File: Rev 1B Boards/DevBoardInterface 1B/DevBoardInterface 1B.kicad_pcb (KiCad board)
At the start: 4 copper layers, 45.6 x 65 mm, 27 parts, among them J11 Banana 2P, J12 Banana 2P, J13 Banana 2P, J3 Conn_01x01_Pin, J6 JST4_F, J9 Conn_01x01_Pin, U10 ADS1014IDGS, U6 ISO164xB, U7 ADS1014IDGS, U8 TLV9301xDBV, U9 DAC53401

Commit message: More layout
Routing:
- net /Dev Board Interface/SCL_{INT}: track 0.00 -> 38.5 mm
- net /+3V3_{DEV}: track 0.00 -> 10.7 mm
- net /Dev Board Interface/SDA_{INT}: track 0.00 -> 10.7 mm
- net /SDA_{IN}: track 0.00 -> 10.4 mm
- net /SCL_{IN}: track 0.00 -> 10.4 mm
- net /+6V_{SCAP}_ADC: track 0.00 -> 9.09 mm
- net GNDPWR: track 0.00 -> 9.06 mm
- net /Dev Board Interface/V_{SC}_scaled: track 0.00 -> 8.17 mm
- net +3V3: track 0.00 -> 4.40 mm
- added copper zone on In2.Cu, net +24V
- added copper zone on F.Cu, net +3V3
- added copper zone on B.Cu, net GND
- added copper zone on In1.Cu, net GND
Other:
- board text added: "+ 24V -"
- board text added: "+ 3V3 -"
- board text added: "+ SCAP -"

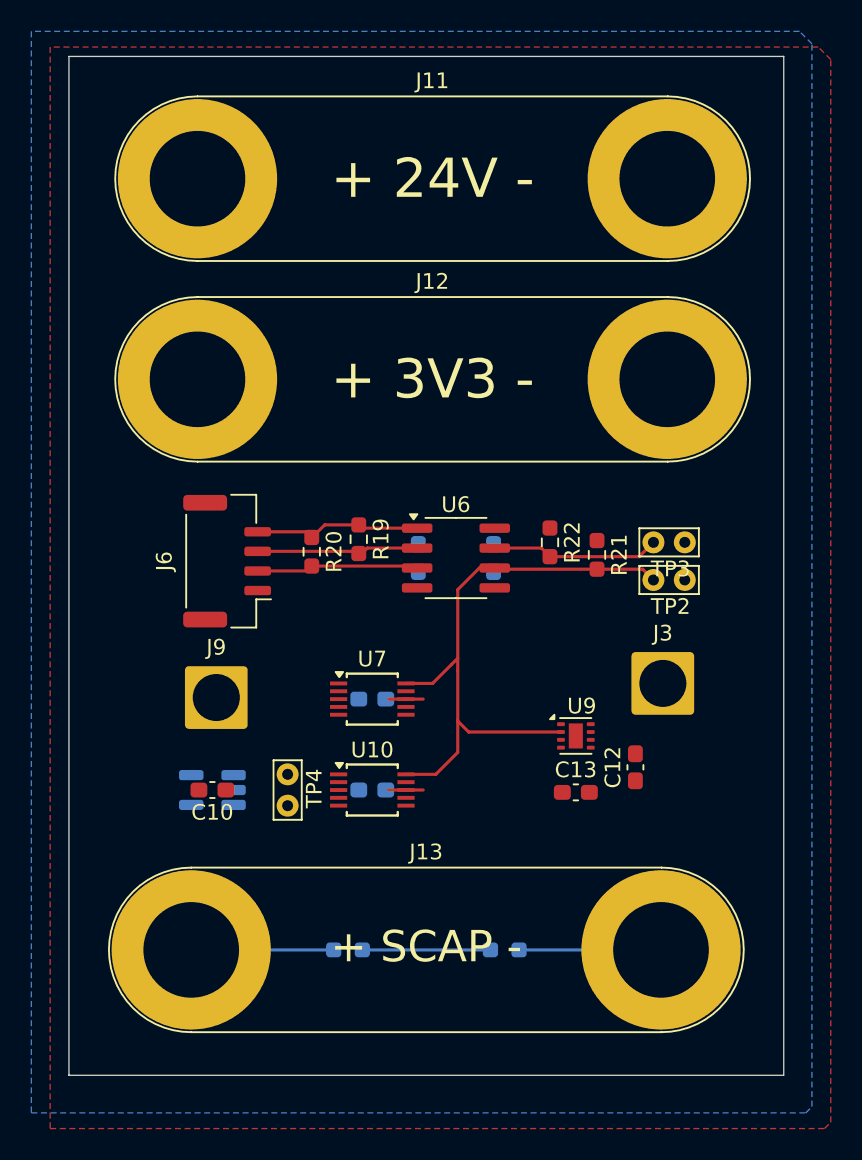
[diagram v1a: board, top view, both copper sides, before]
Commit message: Complete dev board interface layout
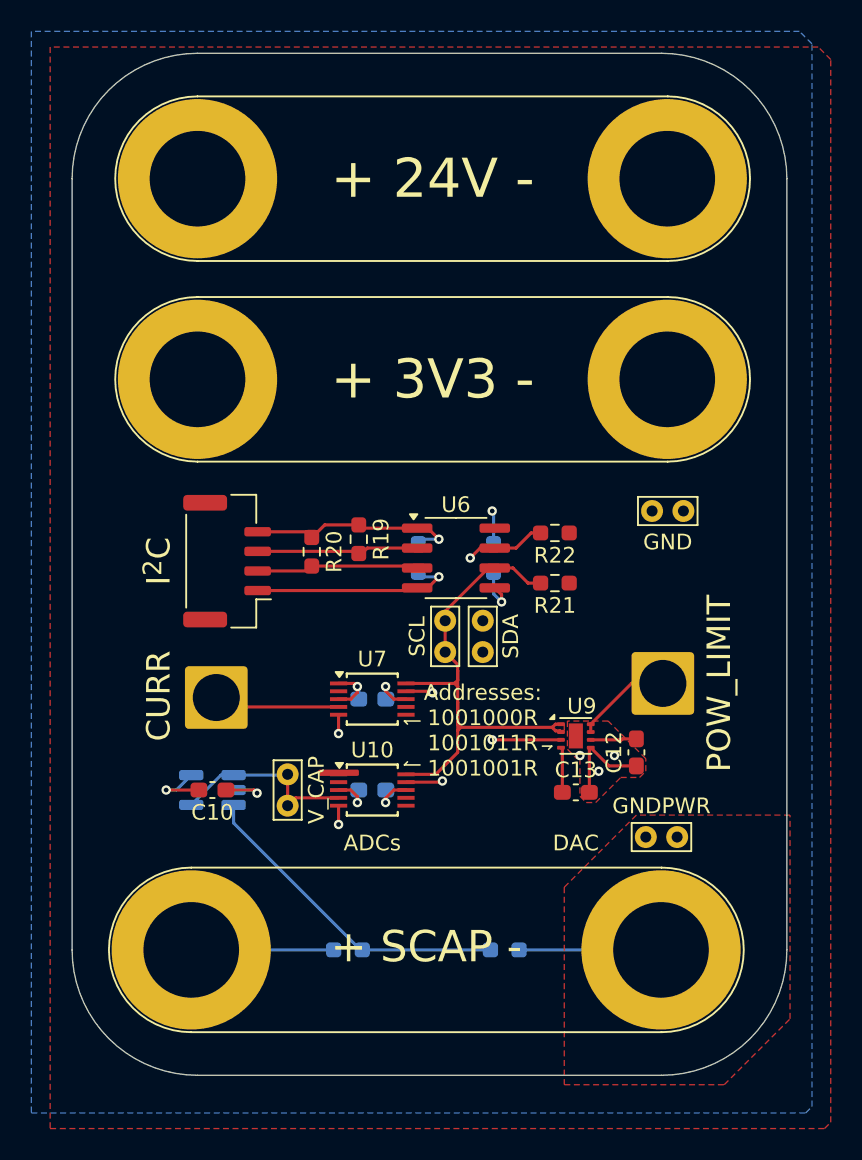
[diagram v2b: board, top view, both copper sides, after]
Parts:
- added G***: LOGO, ! Robomaster Special:StampedeLogo, B.Cu at (178.0, 59.6)
- added TP5: Loop TP, TestPoint:TestPoint_Bridge_Pitch2.0mm_Drill0.7mm, F.Cu at (192.2, 80.2)
- added TP6: Loop TP, TestPoint:TestPoint_Bridge_Pitch2.0mm_Drill0.7mm, F.Cu at (191.8, 101.0)
- moved TP2 14.1 mm to (179.0, 89.2), turned to 90 degrees
- moved TP3 12.9 mm to (181.4, 89.2), turned to 90 degrees
- moved R21 3.23 mm to (186.0, 84.8), turned to 180 degrees
- moved C12 0.95 mm to (191.2, 95.6)
- moved R22 0.68 mm to (186.0, 81.6), turned to 180 degrees
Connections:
- U9 pad 1: +3V3 -> /Dev Board Interface/SCL_{INT}
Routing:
- net GNDPWR: track 9.06 -> 51.5 mm, vias 0 -> 3
- net /Dev Board Interface/SDA_{INT}: track 10.7 -> 35.3 mm, vias 0 -> 4
- net GND: track 0.00 -> 16.0 mm, vias 0 -> 6
- net GNDD: track 0.00 -> 13.4 mm, vias 0 -> 1
- net /Dev Board Interface/V_{SC}_scaled: track 8.17 -> 20.9 mm
- net /Dev Board Interface/V_{SC}_BUF: track 0.00 -> 12.4 mm
- net /CURR_IN: track 0.00 -> 8.05 mm
- net /POW_LIMIT_OUT: track 0.00 -> 6.18 mm
- net +3V3: track 4.40 -> 10.3 mm, vias 0 -> 3
- net /Dev Board Interface/SCL_{INT}: track 38.5 -> 34.3 mm
- net +24V: track 0.00 -> 4.08 mm, vias 0 -> 1
- net /+3V3_{DEV}: track 10.7 -> 13.9 mm, vias 0 -> 1
- net /Dev Board Interface/CAP_{1}: track 0.00 -> 2.89 mm
- added copper zone on F.Cu, net /Dev Board Interface/SCL_{INT}
- added copper zone on F.Cu, net GND
- added copper zone on F.Cu, net GNDPWR
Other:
- board size 45.6 x 65 mm -> 45.6 x 65.2 mm
- board text added: "+3V3 SDA SCL GND"
- board text added: "ADCs"
- board text added: "Addresses: 1001000R 1001011R 1001001R"
- board text added: "CURR"
- board text added: "DAC"
- board text added: "GND"
- board text added: "GNDPWR"
- board text added: "I^{2}C"
- board text added: "POW_LIMIT"
- board text added: "SCL"
- board text added: "SDA"
- board text added: "UT Stampede Supercap Dev Board Interface _{Egan Wang, Jed Wang}"
- board text added: "V_CAP"

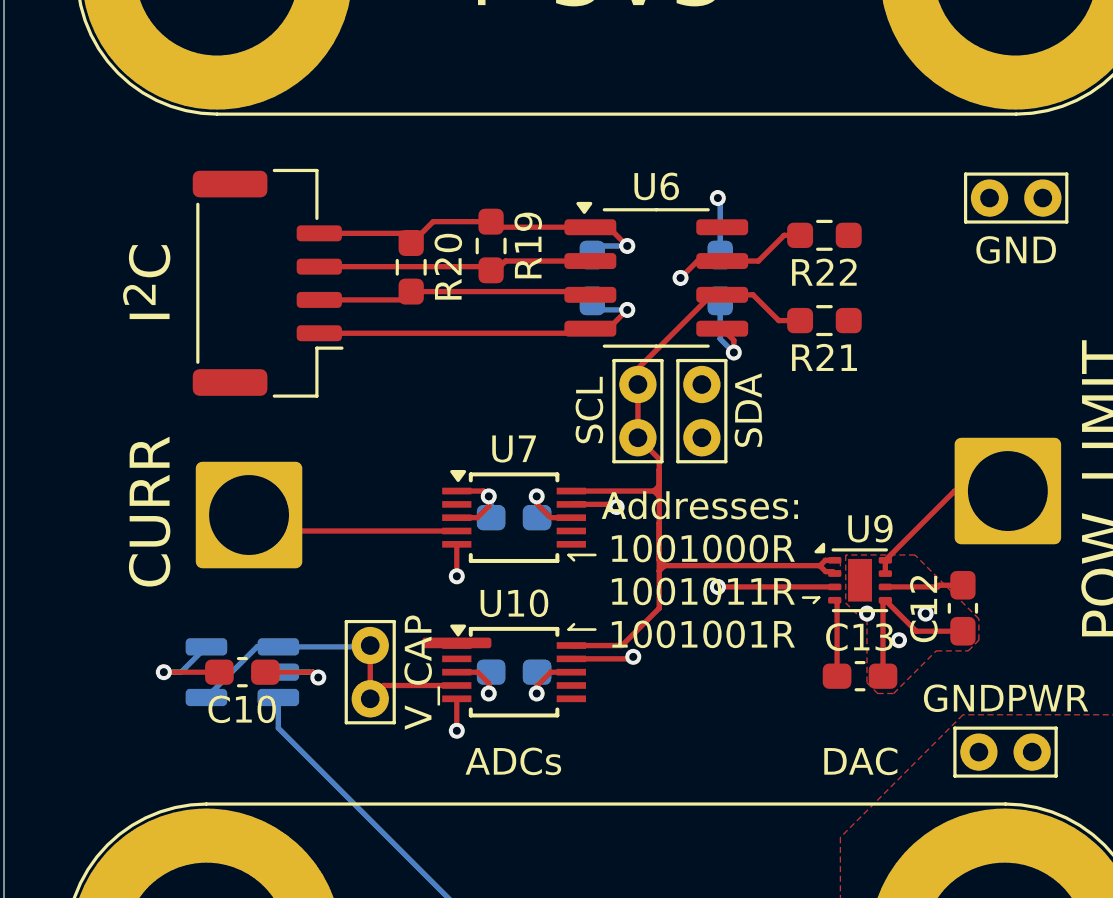
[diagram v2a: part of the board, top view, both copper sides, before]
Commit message: Update PCB to fix ERC breaks
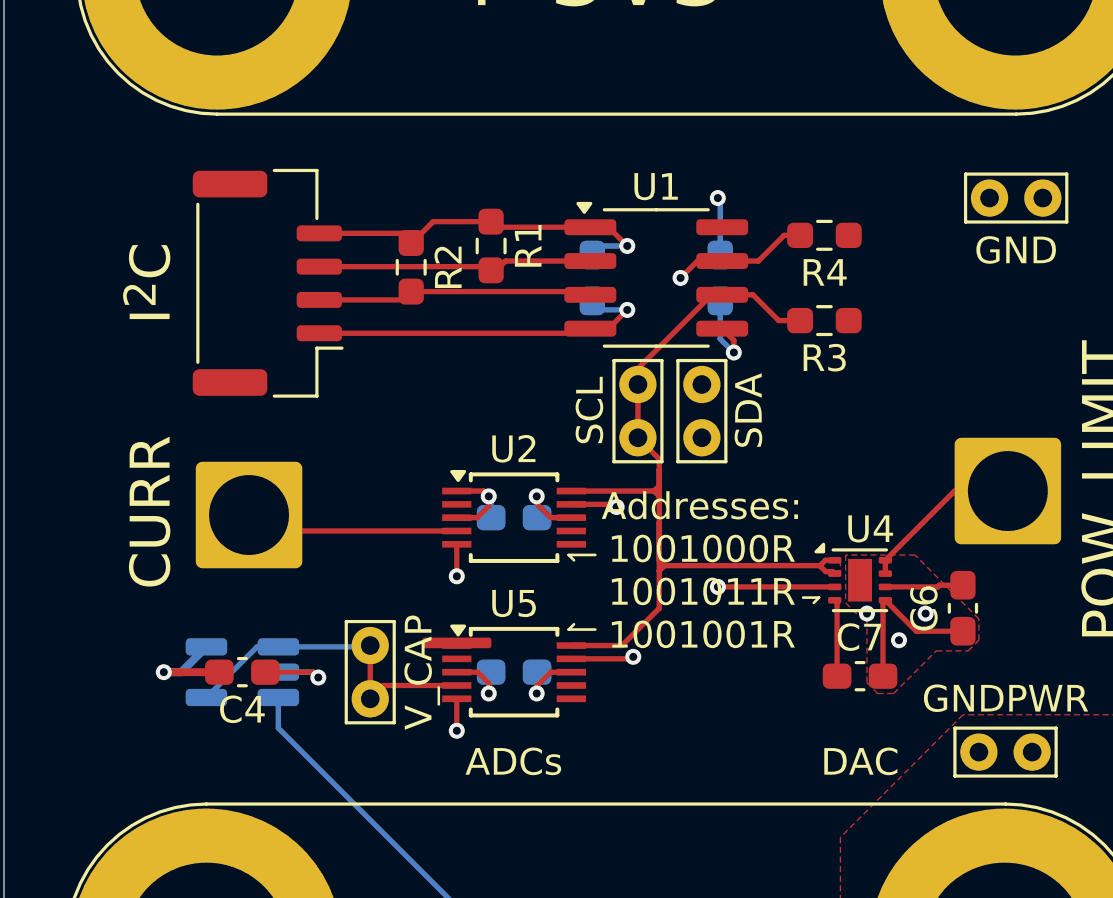
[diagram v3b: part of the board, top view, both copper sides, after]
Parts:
- renumbered C7 to C1, C8 to C2, C9 to C3, C10 to C4, C11 to C5, C12 to C6, C13 to C7, R19 to R1, R20 to R2, R21 to R3, R22 to R4, R23 to R5, R24 to R6, TP2 to TP1, TP3 to TP2, TP4 to TP3, U6 to U1, U7 to U2, U8 to U3, U9 to U4, U10 to U5
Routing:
- net +24V: track 4.08 -> 47.2 mm
- removed copper zone on In2.Cu, net +24V

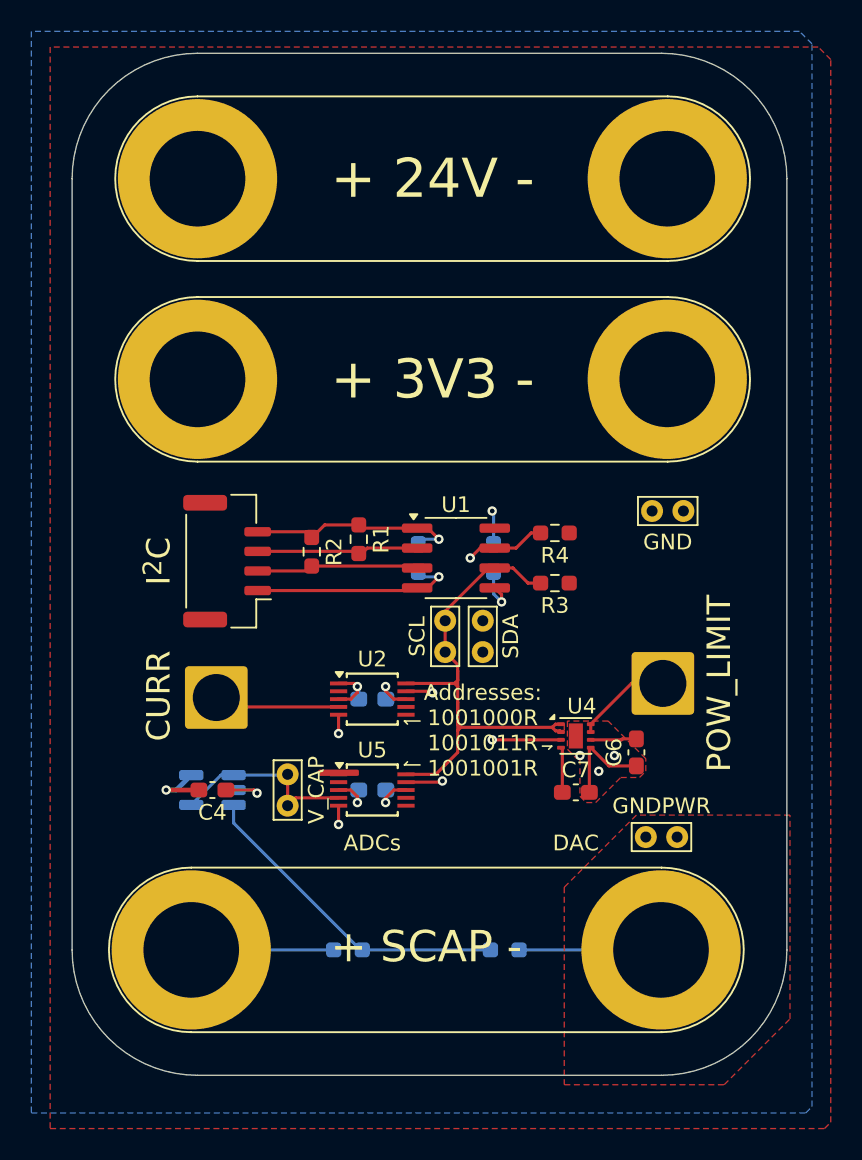
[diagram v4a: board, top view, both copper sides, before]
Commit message: Replace most banana jacks with XT connectors
+ update library
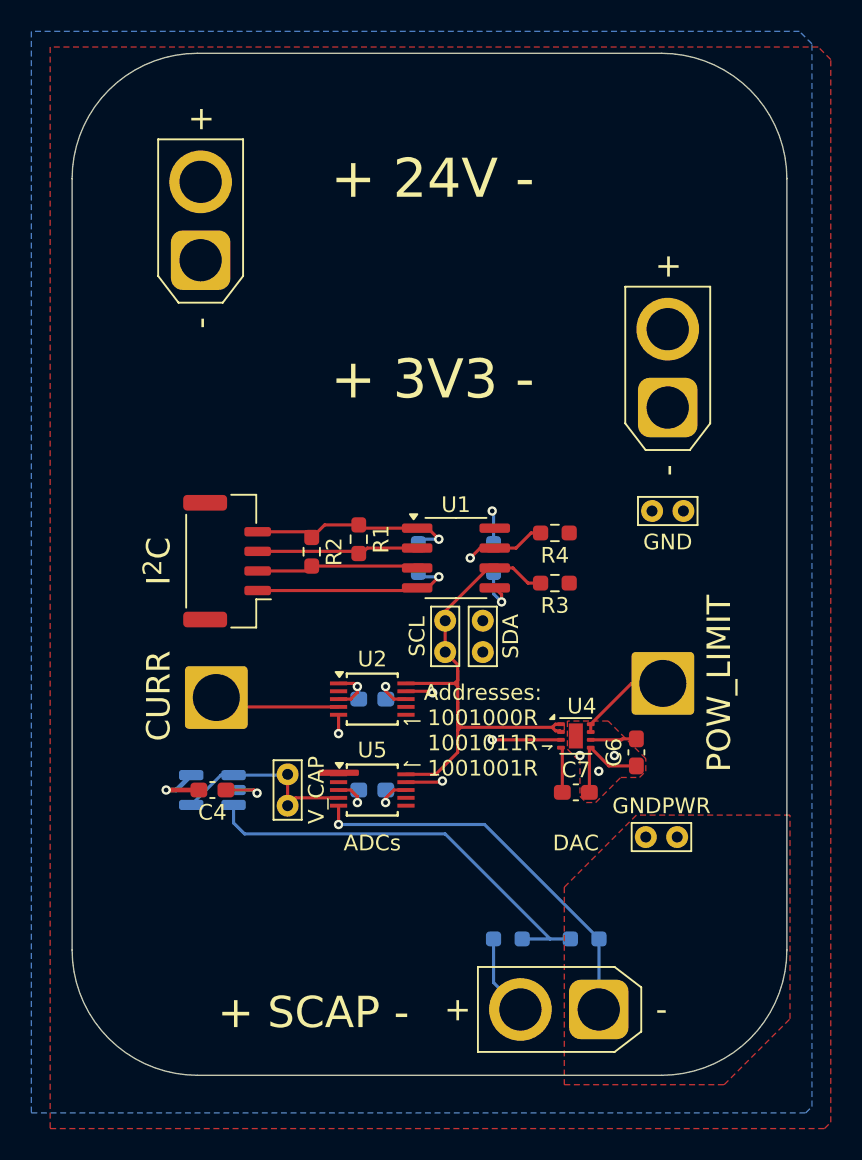
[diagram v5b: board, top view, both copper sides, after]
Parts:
- removed J11, J12, J13: Banana 2P, Connector:Banana_Jack_2Pin
- added J14: XT30_F, Connector_AMASS:AMASS_XT30U-F_1x02_P5.0mm_Vertical, F.Cu at (188.8, 112.0)
- added J15: XT30_F, Connector_AMASS:AMASS_XT30U-F_1x02_P5.0mm_Vertical, F.Cu at (163.4, 64.2)
- added J16: XT30_F, Connector_AMASS:AMASS_XT30U-F_1x02_P5.0mm_Vertical, F.Cu at (193.2, 73.6)
- moved R5 10.2 mm to (183.0, 107.5)
- moved R6 5.15 mm to (187.9, 107.5)
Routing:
- net GNDPWR: track 51.5 -> 42.8 mm
- net /Dev Board Interface/V_{SC}_scaled: track 20.9 -> 27.5 mm
- net /+6V_{SCAP}_ADC: track 9.09 -> 5.21 mm
